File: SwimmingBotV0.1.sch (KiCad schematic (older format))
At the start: 13 parts, among them P1 DCMI, P2 ANALOG

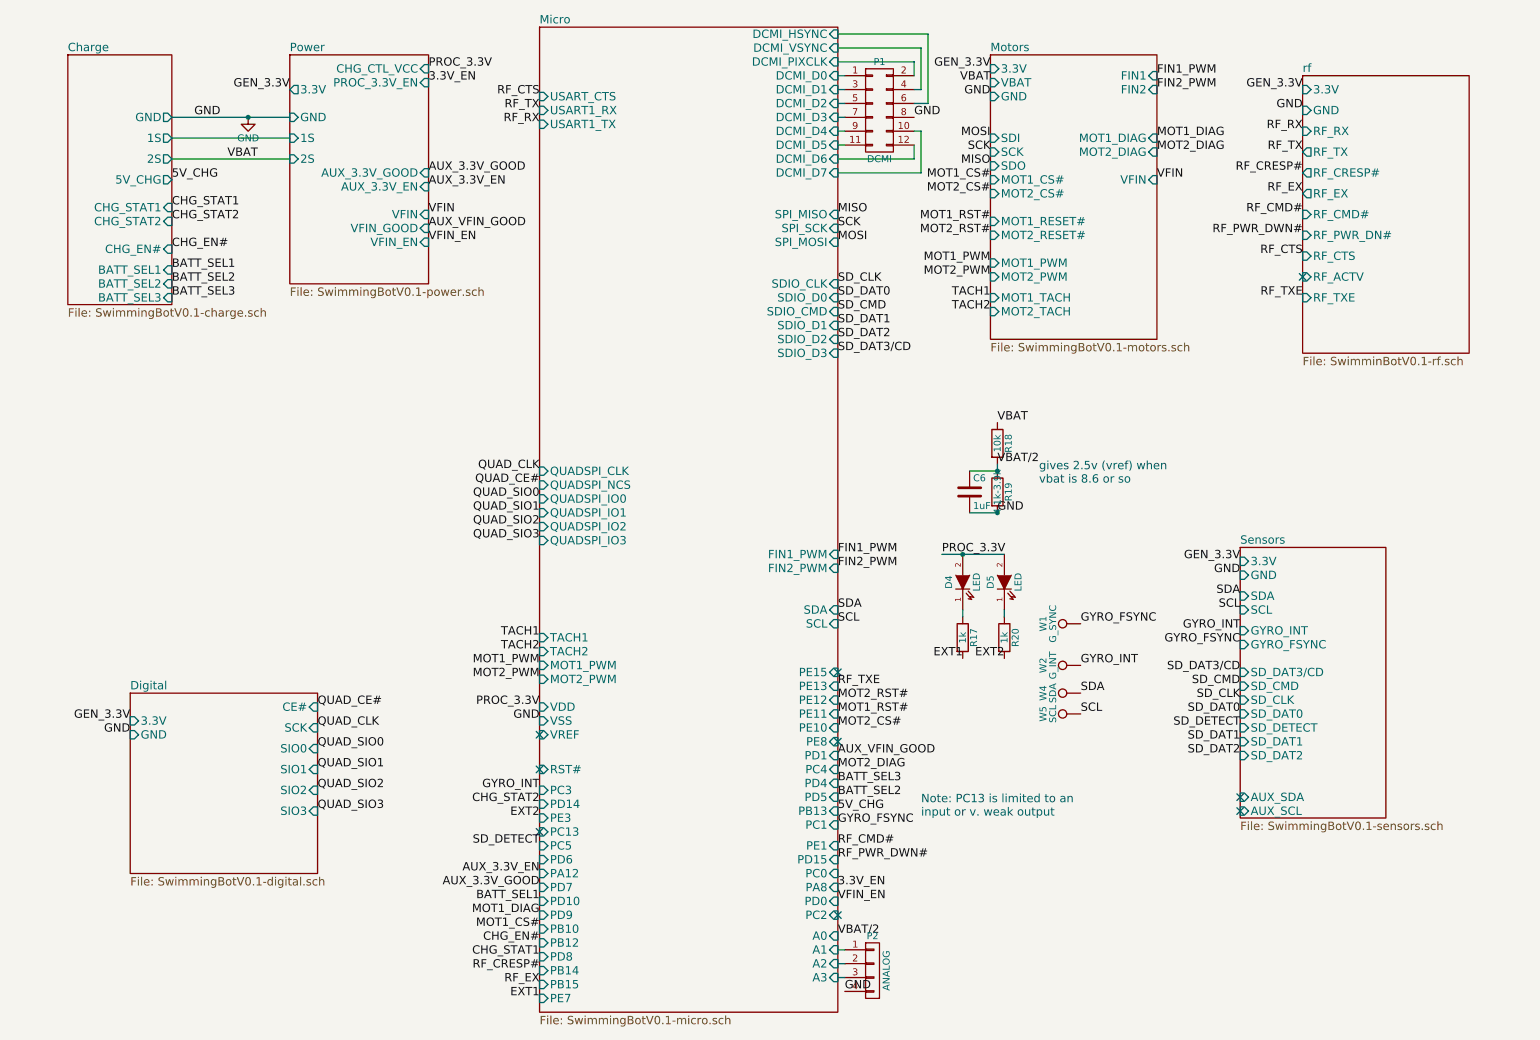
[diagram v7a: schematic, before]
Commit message: rearranged inputs to all be available for unique interrupts, put unused GPIO on a header for later use
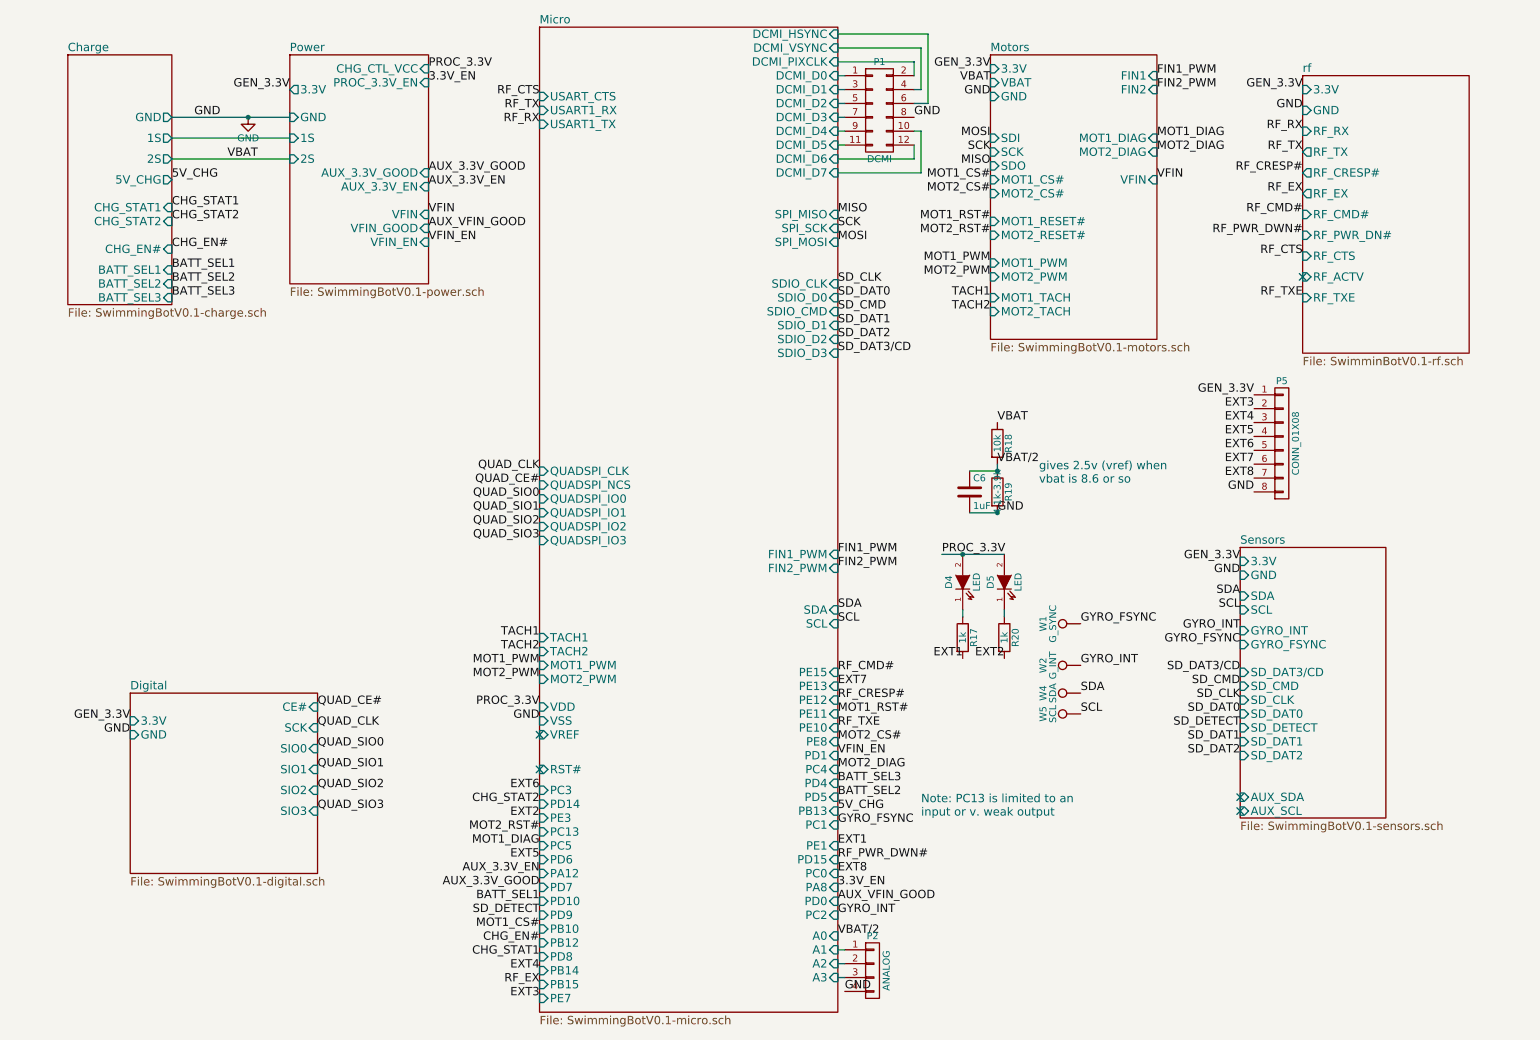
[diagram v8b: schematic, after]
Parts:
- added P5: CONN_01X08, Pin_Headers:Pin_Header_Straight_2x04_Pitch1.27mm, symbol CONN_01X08
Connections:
- net GEN_3.3V: now also P5.1 (P1)
- net GND: now also P5.8 (P8)
- new net EXT3: P5.2 (P2)
- new net EXT4: P5.3 (P3)
- new net EXT5: P5.4 (P4)
- new net EXT6: P5.5 (P5)
- new net EXT7: P5.6 (P6)
- new net EXT8: P5.7 (P7)
- no-connect marks 9 -> 5
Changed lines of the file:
@@
 Text Label 7650 1800 2    60   ~ 0
 MOT2_CS#
-Text Label 6550 5650 0    60   ~ 0
+Text Label 6550 5750 0    60   ~ 0
 MOT2_CS#
 Text Label 4400 7100 2    60   ~ 0
 MOT1_CS#
-Text Label 4400 7400 2    60   ~ 0
+Text Label 6550 5450 0    60   ~ 0
 RF_CRESP#
 Text Label 9900 1800 2    60   ~ 0
@@
 Text Label 4400 7500 2    60   ~ 0
 RF_EX
-Text Label 6550 6500 0    60   ~ 0
+Text Label 6550 5250 0    60   ~ 0
 RF_CMD#
 Text Label 6550 6600 0    60   ~ 0
@@
 Text Label 6550 6350 0    60   ~ 0
 GYRO_FSYNC
-Text Label 4400 6100 2    60   ~ 0
+Text Label 6550 7000 0    60   ~ 0
 GYRO_INT
 Text Label 7650 1400 2    60   ~ 0
@@
 Text Label 6550 5550 0    60   ~ 0
 MOT1_RST#
-Text Label 6550 5450 0    60   ~ 0
+Text Label 4400 6400 2    60   ~ 0
 MOT2_RST#
 Text Label 1750 1900 0    60   ~ 0
@@
 Text Label 9450 5650 2    60   ~ 0
 SD_DETECT
-Text Label 4400 6500 2    60   ~ 0
+Text Label 4400 7000 2    60   ~ 0
 SD_DETECT
 $Sheet
@@
 Text Label 7100 1250 0    60   ~ 0
 GND
-Text Label 4400 7600 2    60   ~ 0
+Text Label 6550 6500 0    60   ~ 0
 EXT1
 Text Label 4400 6300 2    60   ~ 0
@@
 Text Label 8850 1500 0    60   ~ 0
 MOT2_DIAG
-Text Label 4400 7000 2    60   ~ 0
+Text Label 4400 6500 2    60   ~ 0
 MOT1_DIAG
 Text Label 6550 5950 0    60   ~ 0
@@
 Text Label 9900 2550 2    60   ~ 0
 RF_TXE
-Text Label 6550 5350 0    60   ~ 0
+Text Label 6550 5650 0    60   ~ 0
 RF_TXE
 NoConn ~ 9900 2400
@@
 Text Label 3600 2150 0    60   ~ 0
 VFIN_EN
-Text Label 6550 6900 0    60   ~ 0
+Text Label 6550 5850 0    60   ~ 0
 VFIN_EN
 Text Label 3600 1650 0    60   ~ 0
@@
 Text Label 4400 6800 2    60   ~ 0
 AUX_3.3V_GOOD
-Text Label 6550 5850 0    60   ~ 0
+Text Label 6550 6900 0    60   ~ 0
 AUX_VFIN_GOOD
 Text Label 3600 2050 0    60   ~ 0
@@
 Text Label 6550 6050 0    60   ~ 0
 BATT_SEL3
-NoConn ~ 6550 5250
-NoConn ~ 6550 5750
-NoConn ~ 4400 6400
-NoConn ~ 6550 7000
+Text Label 9550 3950 2    60   ~ 0
+GND
+Text Label 9550 3350 2    60   ~ 0
+EXT3
+Text Label 9550 3450 2    60   ~ 0
+EXT4
+Text Label 9550 3550 2    60   ~ 0
+EXT5
+Text Label 9550 3650 2    60   ~ 0
+EXT6
+Text Label 9550 3750 2    60   ~ 0
+EXT7
+Text Label 9550 3850 2    60   ~ 0
+EXT8
+Text Label 4400 7600 2    60   ~ 0
+EXT3
+Text Label 4400 7400 2    60   ~ 0
+EXT4
+Text Label 4400 6600 2    60   ~ 0
+EXT5
+Text Label 4400 6100 2    60   ~ 0
+EXT6
+Text Label 6550 5350 0    60   ~ 0
+EXT7
+Text Label 6550 6700 0    60   ~ 0
+EXT8
+$Comp
+L CONN_01X08 P5
+U 1 1 579A90D9
+P 9750 3600
+F 0 "P5" H 9750 4050 50  0000 C CNN
+F 1 "CONN_01X08" V 9850 3600 50  0000 C CNN
+F 2 "Pin_Headers:Pin_Header_Straight_2x04_Pitch1.27mm" H 9750 3600 50  0001 C CNN
+F 3 "" H 9750 3600 50  0000 C CNN
+	1    9750 3600
+	1    0    0    -1
+$EndComp
+Text Label 9550 3250 2    60   ~ 0
+GEN_3.3V
 $EndSCHEMATC
